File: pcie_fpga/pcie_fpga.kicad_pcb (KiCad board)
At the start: 4 copper layers, 167.7 x 68.9 mm, 4 parts, among them J2 PCIexpress_x8, U2 XCAU10P-1FFVB676I, X1 ECS-2520MVQ-1000-BN-TR

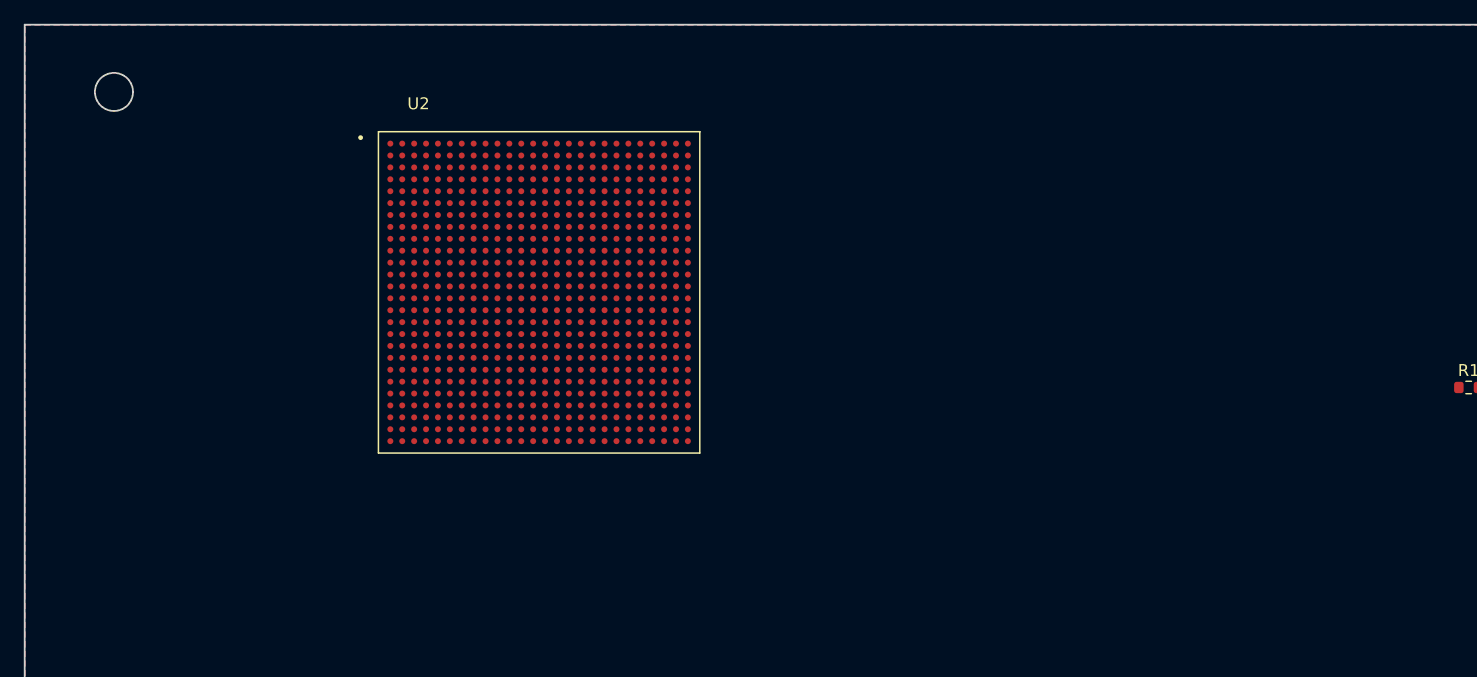
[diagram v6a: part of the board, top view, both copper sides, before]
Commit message: added PMOD and JTAG connectors
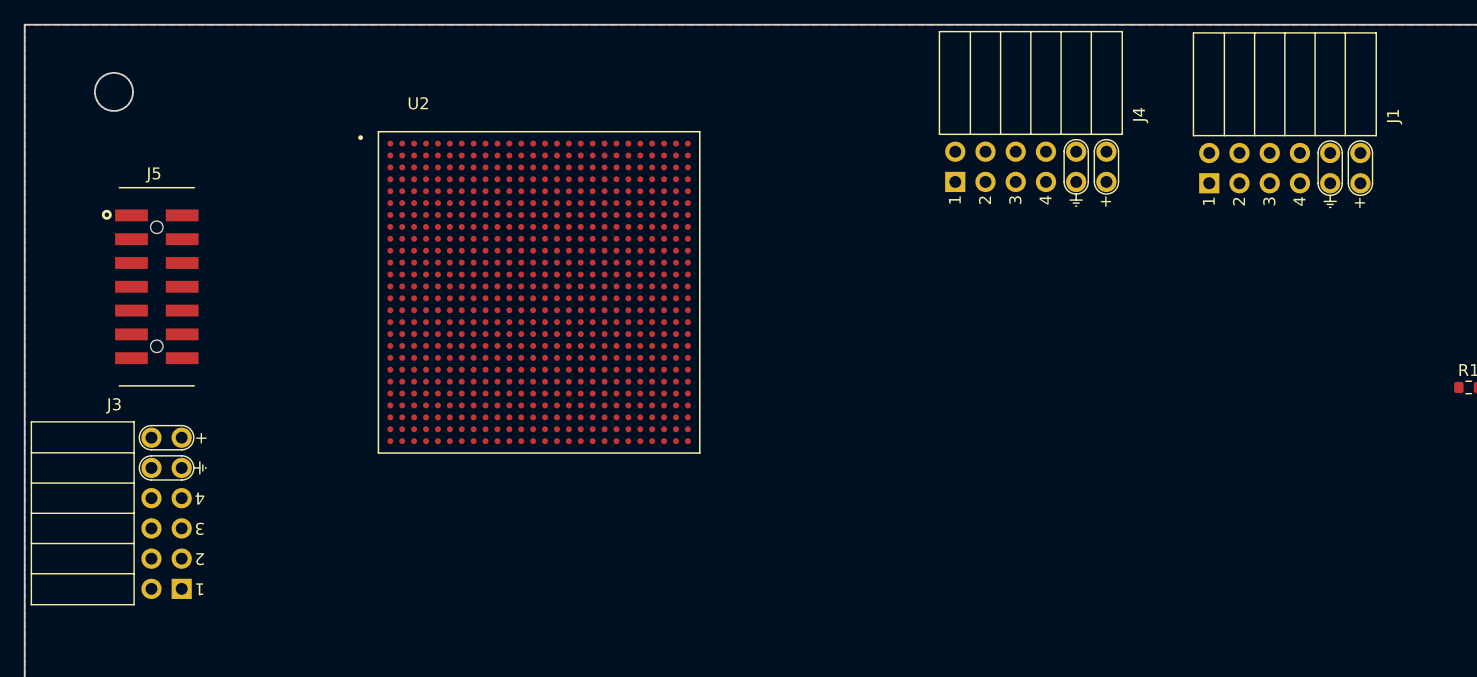
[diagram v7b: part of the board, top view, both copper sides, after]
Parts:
- added J1: PMOD_Host_Conn_02x06, pedrolib:PMOD_PinSocket_2x06_P2.54mm_Horizontal, F.Cu at (164.0, 138.5)
- added J3: PMOD_Host_Conn_02x06, pedrolib:PMOD_PinSocket_2x06_P2.54mm_Horizontal, F.Cu at (77.7, 172.6)
- added J4: PMOD_Host_Conn_02x06, pedrolib:PMOD_PinSocket_2x06_P2.54mm_Horizontal, F.Cu at (142.7, 138.4)
- added J5: 87832-1420, pedrolib:MOLEX_87832-1420, F.Cu at (75.6, 147.2)

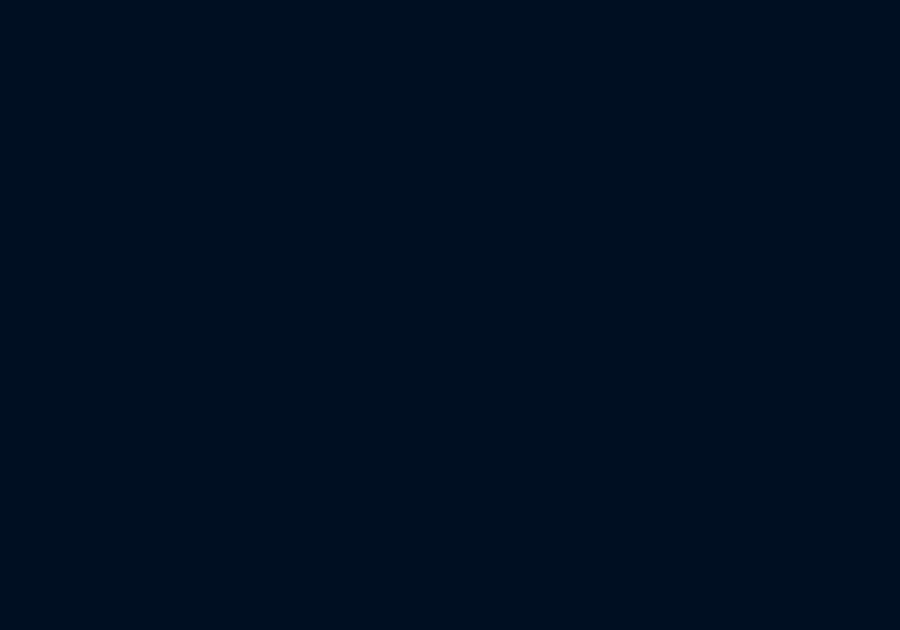
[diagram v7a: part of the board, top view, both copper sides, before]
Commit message: wired pcie links with ac coupling caps
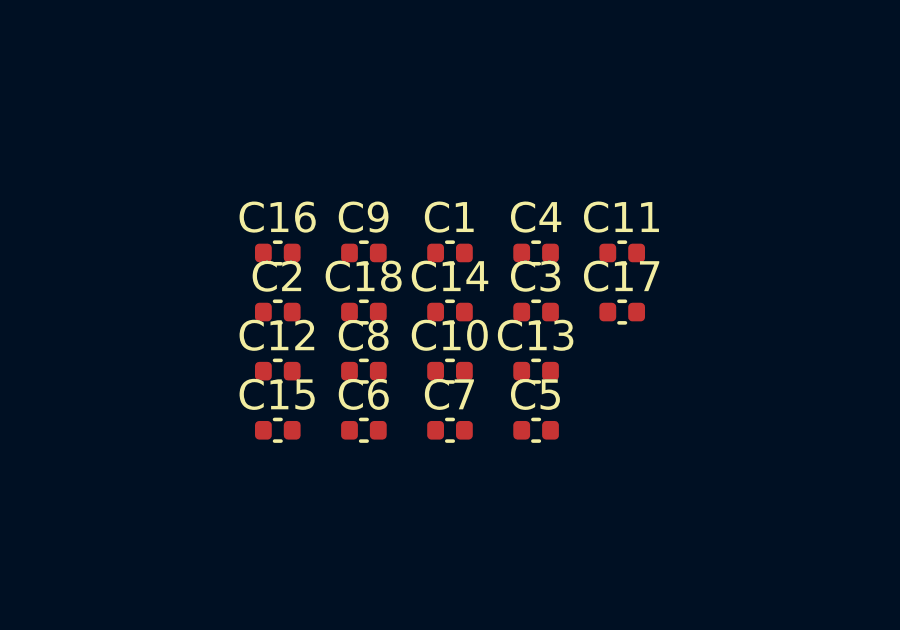
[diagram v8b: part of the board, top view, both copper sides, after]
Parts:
- added C1: 0.01uf, Capacitor_SMD:C_0402_1005Metric, F.Cu at (143.8, 164.7)
- added C10: 0.01uf, Capacitor_SMD:C_0402_1005Metric, F.Cu at (143.8, 168.7)
- added C11: 0.01uf, Capacitor_SMD:C_0402_1005Metric, F.Cu at (149.6, 164.7)
- added C12: 0.01uf, Capacitor_SMD:C_0402_1005Metric, F.Cu at (138.1, 168.7)
- added C13: 0.01uf, Capacitor_SMD:C_0402_1005Metric, F.Cu at (146.7, 168.7)
- added C14: 0.01uf, Capacitor_SMD:C_0402_1005Metric, F.Cu at (143.8, 166.7)
- added C15: 0.01uf, Capacitor_SMD:C_0402_1005Metric, F.Cu at (138.1, 170.7)
- added C16: 0.01uf, Capacitor_SMD:C_0402_1005Metric, F.Cu at (138.1, 164.7)
- added C17: 0.01uf, Capacitor_SMD:C_0402_1005Metric, F.Cu at (149.6, 166.7)
- added C18: 0.01uf, Capacitor_SMD:C_0402_1005Metric, F.Cu at (141.0, 166.7)
- added C2: 0.01uf, Capacitor_SMD:C_0402_1005Metric, F.Cu at (138.1, 166.7)
- added C3: 0.01uf, Capacitor_SMD:C_0402_1005Metric, F.Cu at (146.7, 166.7)
- added C4: 0.01uf, Capacitor_SMD:C_0402_1005Metric, F.Cu at (146.7, 164.7)
- added C5: 0.01uf, Capacitor_SMD:C_0402_1005Metric, F.Cu at (146.7, 170.7)
- added C6: 0.01uf, Capacitor_SMD:C_0402_1005Metric, F.Cu at (141.0, 170.7)
- added C7: 0.01uf, Capacitor_SMD:C_0402_1005Metric, F.Cu at (143.8, 170.7)
- added C8: 0.01uf, Capacitor_SMD:C_0402_1005Metric, F.Cu at (141.0, 168.7)
- added C9: 0.01uf, Capacitor_SMD:C_0402_1005Metric, F.Cu at (141.0, 164.7)
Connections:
- U2 pad AA4: unconnected-(U2-PadAA4) -> /pre_per4_N
- U2 pad AA5: unconnected-(U2-PadAA5) -> /pre_per4_P
- U2 pad AB1: unconnected-(U2-PadAB1) -> /pet3_N
- U2 pad AB2: unconnected-(U2-PadAB2) -> /pet3_P
- U2 pad AC4: unconnected-(U2-PadAC4) -> /pre_per3_N
- U2 pad AC5: unconnected-(U2-PadAC5) -> /pre_per3_P
- U2 pad AD1: unconnected-(U2-PadAD1) -> /pet2_N
- U2 pad AD2: unconnected-(U2-PadAD2) -> /pet2_P
- U2 pad AD6: unconnected-(U2-PadAD6) -> /pre_per2_N
- U2 pad AD7: unconnected-(U2-PadAD7) -> /pre_per2_P
- U2 pad AE3: unconnected-(U2-PadAE3) -> /pet1_N
- U2 pad AE4: unconnected-(U2-PadAE4) -> /pet1_P
- U2 pad AE8: unconnected-(U2-PadAE8) -> /pre_per1_N
- U2 pad AE9: unconnected-(U2-PadAE9) -> /pre_per1_P
- U2 pad AF1: unconnected-(U2-PadAF1) -> /pet0_N
- U2 pad AF2: unconnected-(U2-PadAF2) -> /pet0_P
- U2 pad AF6: unconnected-(U2-PadAF6) -> /pre_per0_N
- U2 pad AF7: unconnected-(U2-PadAF7) -> /pre_per0_P
- U2 pad P1: unconnected-(U2-PadP1) -> /pet7_N
- U2 pad P2: unconnected-(U2-PadP2) -> /pet7_P
- U2 pad R4: unconnected-(U2-PadR4) -> /pre_per7_N
- U2 pad R5: unconnected-(U2-PadR5) -> /pre_per7_P
- U2 pad T1: unconnected-(U2-PadT1) -> /pet6_N
- U2 pad T2: unconnected-(U2-PadT2) -> /pet6_P
- U2 pad U4: unconnected-(U2-PadU4) -> /pre_per6_N
- U2 pad U5: unconnected-(U2-PadU5) -> /pre_per6_P
- U2 pad V1: unconnected-(U2-PadV1) -> /pet5_N
- U2 pad V2: unconnected-(U2-PadV2) -> /pet5_P
- U2 pad V6: unconnected-(U2-PadV6) -> /ac_refclk_N
- U2 pad V7: unconnected-(U2-PadV7) -> /ac_refclk_P
- U2 pad W4: unconnected-(U2-PadW4) -> /pre_per5_N
- U2 pad W5: unconnected-(U2-PadW5) -> /pre_per5_P
- U2 pad Y1: unconnected-(U2-PadY1) -> /pet4_N
- U2 pad Y2: unconnected-(U2-PadY2) -> /pet4_P
